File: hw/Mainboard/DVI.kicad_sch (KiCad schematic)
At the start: 18 parts, among them J12 NOT_HDMI_A

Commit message: hw: routing / silk wip
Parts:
- removed JP7: DVI_CEC, Jumper:SolderJumper-2_P1.3mm_Open_RoundedPad1.0x1.5mm, symbol Jumper:SolderJumper_2_Open
- removed JP8: DVI_SCL, Jumper:SolderJumper-2_P1.3mm_Open_RoundedPad1.0x1.5mm, symbol Jumper:SolderJumper_2_Open
- removed JP9: DVI_SDA, Jumper:SolderJumper-2_P1.3mm_Open_RoundedPad1.0x1.5mm, symbol Jumper:SolderJumper_2_Open
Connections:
- net HDMI_SCL is gone; now on net SCL: J12.15 (SCL), R8.2
- net HDMI_SDA is gone; now on net SDA: J12.16 (SDA), R9.2
- net CEC: now also R16.1, R7.2
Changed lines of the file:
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@@
-    (stroke (width 0) (type default) (color 0 0 0 0))
-  )
-  (wire (pts (xy 111.76 101.6) (xy 129.54 101.6))
     (stroke (width 0) (type default) (color 0 0 0 0))
   )
@@
     (stroke (width 0) (type default) (color 0 0 0 0))
   )
-  (wire (pts (xy 111.76 91.44) (xy 124.46 91.44))
-    (stroke (width 0) (type default) (color 0 0 0 0))
-  )
   (wire (pts (xy 167.64 68.58) (xy 180.34 68.58))
     (stroke (width 0) (type default) (color 0 0 0 0))
   )
-  (wire (pts (xy 97.79 101.6) (xy 104.14 101.6))
+  (wire (pts (xy 97.79 101.6) (xy 129.54 101.6))
     (stroke (width 0) (type default) (color 0 0 0 0))
   )
@@
     (stroke (width 0) (type default) (color 0 0 0 0))
   )
-  (wire (pts (xy 97.79 111.76) (xy 104.14 111.76))
-    (stroke (width 0) (type default) (color 0 0 0 0))
-  )
   (bus (pts (xy 146.05 66.04) (xy 146.05 68.58))
     (stroke (width 0) (type default) (color 0 0 0 0))
@@
     (stroke (width 0) (type default) (color 0 0 0 0))
   )
-  (wire (pts (xy 111.76 111.76) (xy 134.62 111.76))
+  (wire (pts (xy 97.79 111.76) (xy 134.62 111.76))
     (stroke (width 0) (type default) (color 0 0 0 0))
   )
@@
     (stroke (width 0) (type default) (color 0 0 0 0))
   )
-  (wire (pts (xy 97.79 91.44) (xy 104.14 91.44))
+  (wire (pts (xy 97.79 91.44) (xy 124.46 91.44))
     (stroke (width 0) (type default) (color 0 0 0 0))
   )
@@
     )
     (pin "1")
-  )
-  (symbol (lib_id "Jumper:SolderJumper_2_Open") (at 107.95 101.6 0) (unit 1)
-    (in_bom yes) (on_board yes) (fields_autoplaced)
-    (property "Reference" "JP8" (id 0) (at 107.95 95.25 0))
-    (property "Value" "DVI_SCL" (id 1) (at 107.95 97.79 0))
-    (property "Footprint" "Jumper:SolderJumper-2_P1.3mm_Open_RoundedPad1.0x1.5mm" (id 2) (at 107.95 101.6 0)
-      (effects (font (size 1.27 1.27)) hide)
-    )
-    (property "Datasheet" "~" (id 3) (at 107.95 101.6 0)
-      (effects (font (size 1.27 1.27)) hide)
-    )
-    (pin "1")
-    (pin "2")
   )
   (symbol (lib_id "PET:PowerTie_2") (at 194.31 59.69 180) (unit 1)
@@
     (pin "2")
   )
-  (symbol (lib_id "Jumper:SolderJumper_2_Open") (at 107.95 91.44 0) (unit 1)
-    (in_bom yes) (on_board yes) (fields_autoplaced)
-    (property "Reference" "JP7" (id 0) (at 107.95 85.09 0))
-    (property "Value" "DVI_CEC" (id 1) (at 107.95 87.63 0))
-    (property "Footprint" "Jumper:SolderJumper-2_P1.3mm_Open_RoundedPad1.0x1.5mm" (id 2) (at 107.95 91.44 0)
-      (effects (font (size 1.27 1.27)) hide)
-    )
-    (property "Datasheet" "~" (id 3) (at 107.95 91.44 0)
-      (effects (font (size 1.27 1.27)) hide)
-    )
-    (pin "1")
-    (pin "2")
-  )
   (symbol (lib_id "Device:R_Small") (at 165.1 86.36 90) (unit 1)
     (in_bom yes) (on_board yes)
@@
       (effects (font (size 1.27 1.27)) hide)
     )
-    (pin "1")
-    (pin "2")
-  )
-  (symbol (lib_id "Jumper:SolderJumper_2_Open") (at 107.95 111.76 0) (unit 1)
-    (in_bom yes) (on_board yes) (fields_autoplaced)
-    (property "Reference" "JP9" (id 0) (at 107.95 105.41 0))
-    (property "Value" "DVI_SDA" (id 1) (at 107.95 107.95 0))
-    (property "Footprint" "Jumper:SolderJumper-2_P1.3mm_Open_RoundedPad1.0x1.5mm" (id 2) (at 107.95 111.76 0)
-      (effects (font (size 1.27 1.27)) hide)
-    )
-    (property "Datasheet" "~" (id 3) (at 107.95 111.76 0)
-      (effects (font (size 1.27 1.27)) hide)
-    )

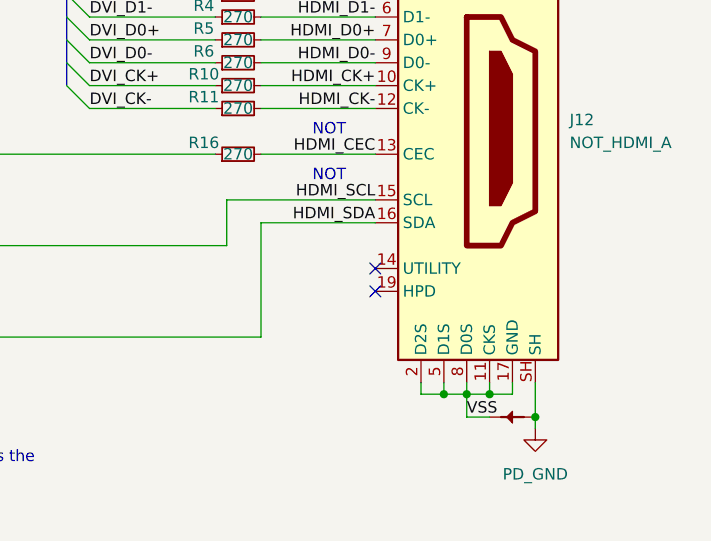
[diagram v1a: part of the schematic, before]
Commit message: hw: heat sink, trace size, more stitching
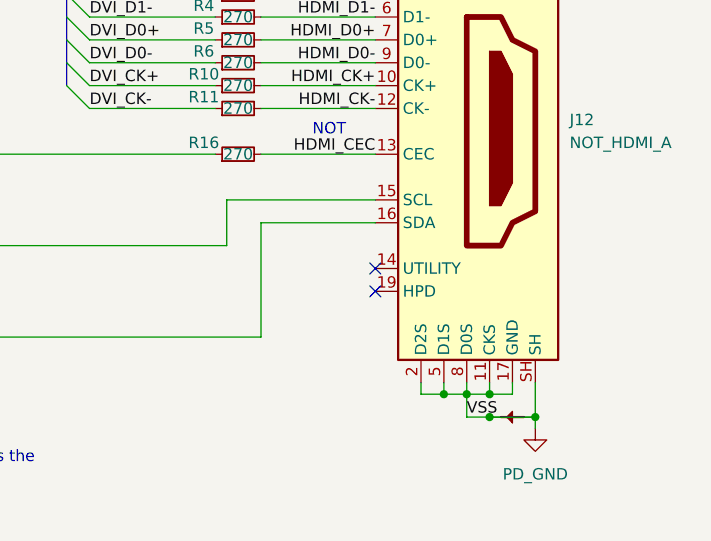
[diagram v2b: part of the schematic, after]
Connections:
- net VSS is gone; now on net PD_GND: J12.11 (CKS), J12.17 (GND), J12.2 (D2S), J12.5 (D1S), J12.8 (D0S), PT37.2
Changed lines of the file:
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@@
   (junction (at 134.62 111.76) (diameter 0) (color 0 0 0 0)
+  )
+  (junction (at 193.04 120.65) (diameter 0) (color 0 0 0 0)
   )
   (junction (at 193.04 118.11) (diameter 0) (color 0 0 0 0)
@@
     (stroke (width 0) (type default) (color 0 0 0 0))
   )
+  (wire (pts (xy 193.04 120.65) (xy 198.12 120.65))
+    (stroke (width 0) (type default) (color 0 0 0 0))
+  )
   (wire (pts (xy 163.83 101.6) (xy 163.83 96.52))
     (stroke (width 0) (type default) (color 0 0 0 0))
@@
   (wire (pts (xy 198.12 59.69) (xy 196.85 59.69))
     (stroke (width 0) (type default) (color 0 0 0 0))
-  )
-  (text "NOT" (at 173.355 94.615 0)
-    (effects (font (size 1.27 1.27)) (justify left bottom))
   )
   (text "NOT" (at 172.72 66.675 0)
@@
     (effects (font (size 1.27 1.27)) (justify right bottom))
   )
-  (label "HDMI_SCL" (at 180.34 96.52 180)
-    (effects (font (size 1.27 1.27)) (justify right bottom))
-  )
   (label "VSS" (at 190.5 120.65 0)
     (effects (font (size 1.27 1.27)) (justify left bottom))
@@
     (effects (font (size 1.27 1.27)) (justify left bottom))
   )
-  (label "HDMI_SDA" (at 180.34 99.06 180)
-    (effects (font (size 1.27 1.27)) (justify right bottom))
-  )
   (label "HDMI_D2+" (at 180.34 68.58 180)

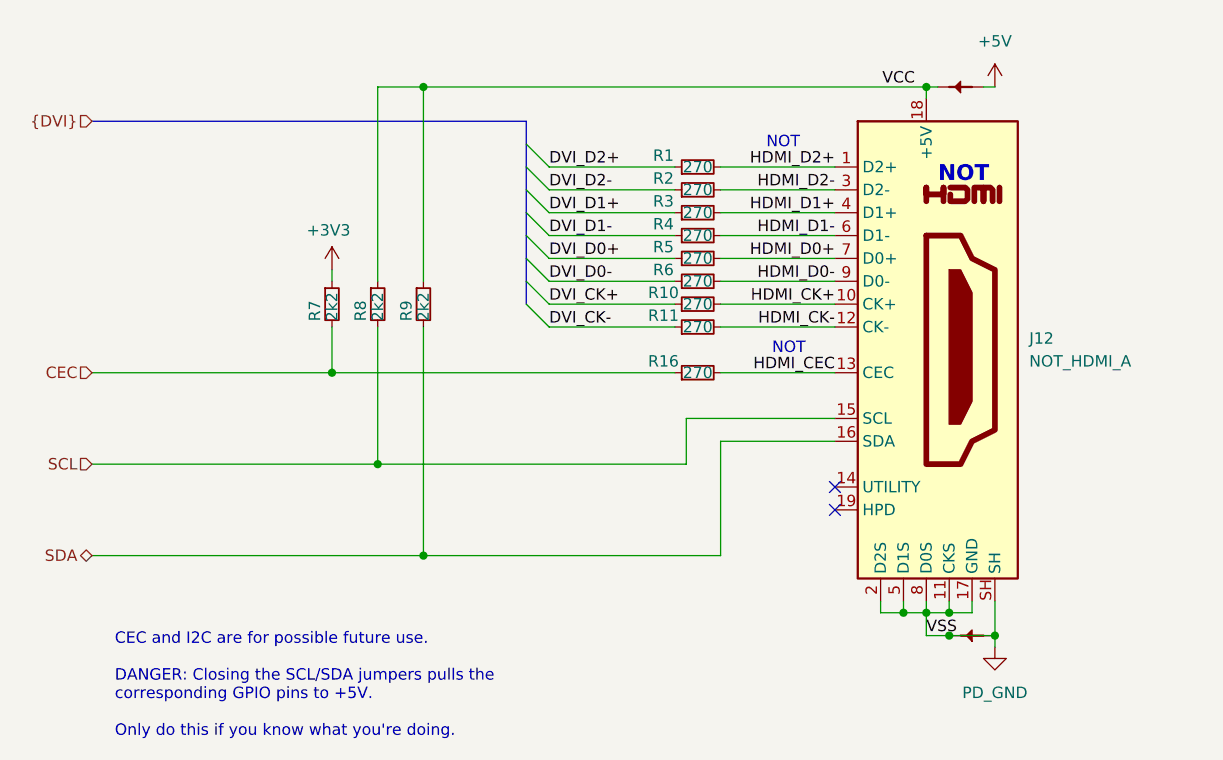
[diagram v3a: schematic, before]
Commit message: hw: 9V DC plug on left edge, change default track size
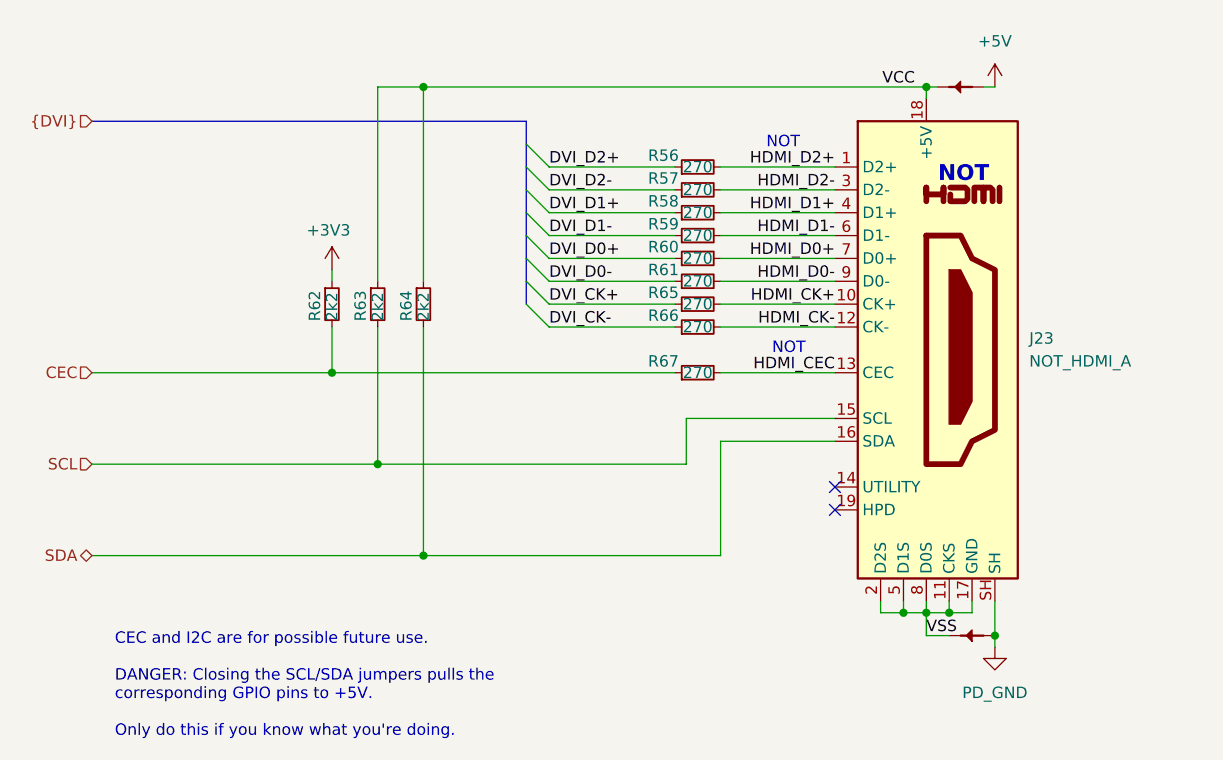
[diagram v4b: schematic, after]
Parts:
- renumbered J12 to J23, PT18 to PT49, PT37 to PT50, R1 to R56, R2 to R57, R3 to R58, R4 to R59, R5 to R60, R6 to R61, R7 to R62, R8 to R63, R9 to R64, R10 to R65, R11 to R66, R16 to R67
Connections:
- net PD_GND: no longer J23.11 (CKS), J23.17 (GND), J23.2 (D2S), J23.5 (D1S), J23.8 (D0S), PT50.2
- new net VSS: J23.11 (CKS), J23.17 (GND), J23.2 (D2S), J23.5 (D1S), J23.8 (D0S), PT50.2
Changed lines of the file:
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@@
   (junction (at 134.62 111.76) (diameter 0) (color 0 0 0 0)
-  )
-  (junction (at 193.04 120.65) (diameter 0) (color 0 0 0 0)
   )
   (junction (at 193.04 118.11) (diameter 0) (color 0 0 0 0)
@@
     (stroke (width 0) (type default) (color 0 0 0 0))
   )
-  (wire (pts (xy 193.04 120.65) (xy 198.12 120.65))
-    (stroke (width 0) (type default) (color 0 0 0 0))
-  )
   (wire (pts (xy 163.83 101.6) (xy 163.83 96.52))
     (stroke (width 0) (type default) (color 0 0 0 0))
@@
   (symbol (lib_id "Device:R_Small") (at 165.1 83.82 90) (unit 1)
     (in_bom yes) (on_board yes)
-    (property "Reference" "R10" (id 0) (at 161.29 82.55 90))
+    (property "Reference" "R65" (id 0) (at 161.29 82.55 90))
     (property "Value" "270" (id 1) (at 165.1 83.82 90))
     (property "Footprint" "Resistor_SMD:R_0603_1608Metric" (id 2) (at 165.1 83.82 0)
@@
   (symbol (lib_id "Device:R_Small") (at 165.1 76.2 90) (unit 1)
     (in_bom yes) (on_board yes)
-    (property "Reference" "R4" (id 0) (at 161.29 74.93 90))
+    (property "Reference" "R59" (id 0) (at 161.29 74.93 90))
     (property "Value" "270" (id 1) (at 165.1 76.2 90))
     (property "Footprint" "Resistor_SMD:R_0603_1608Metric" (id 2) (at 165.1 76.2 0)
@@
   (symbol (lib_id "Device:R_Small") (at 134.62 83.82 0) (unit 1)
     (in_bom yes) (on_board yes)
-    (property "Reference" "R9" (id 0) (at 132.715 85.725 90)
+    (property "Reference" "R64" (id 0) (at 132.715 85.725 90)
       (effects (font (size 1.27 1.27)) (justify left))
     )
@@
   (symbol (lib_id "PET:PowerTie_2") (at 195.58 120.65 180) (unit 1)
     (in_bom yes) (on_board yes) (fields_autoplaced)
-    (property "Reference" "PT37" (id 0) (at 195.58 122.555 0)
+    (property "Reference" "PT50" (id 0) (at 195.58 122.555 0)
       (effects (font (size 1.27 1.27)) hide)
     )
@@
   (symbol (lib_id "Device:R_Small") (at 129.54 83.82 0) (unit 1)
     (in_bom yes) (on_board yes)
-    (property "Reference" "R8" (id 0) (at 127.635 85.725 90)
+    (property "Reference" "R63" (id 0) (at 127.635 85.725 90)
       (effects (font (size 1.27 1.27)) (justify left))
     )
@@
   (symbol (lib_id "power:+5V") (at 198.12 59.69 0) (unit 1)
     (in_bom yes) (on_board yes) (fields_autoplaced)
-    (property "Reference" "#PWR0144" (id 0) (at 198.12 63.5 0)
+    (property "Reference" "#PWR0141" (id 0) (at 198.12 63.5 0)
       (effects (font (size 1.27 1.27)) hide)
     )
@@
   (symbol (lib_id "PET:PowerTie_2") (at 194.31 59.69 180) (unit 1)
     (in_bom yes) (on_board yes) (fields_autoplaced)
-    (property "Reference" "PT18" (id 0) (at 194.31 61.595 0)
+    (property "Reference" "PT49" (id 0) (at 194.31 61.595 0)
       (effects (font (size 1.27 1.27)) hide)
     )
@@
   (symbol (lib_id "power:+3V3") (at 124.46 80.01 0) (mirror y) (unit 1)
     (in_bom yes) (on_board yes)
-    (property "Reference" "#PWR0145" (id 0) (at 124.46 83.82 0)
+    (property "Reference" "#PWR0142" (id 0) (at 124.46 83.82 0)
       (effects (font (size 1.27 1.27)) hide)
     )
@@
   (symbol (lib_id "Connector:HDMI_A") (at 190.5 88.9 0) (unit 1)
     (in_bom yes) (on_board yes)
-    (property "Reference" "J12" (id 0) (at 201.93 87.63 0)
+    (property "Reference" "J23" (id 0) (at 201.93 87.63 0)
       (effects (font (size 1.27 1.27)) (justify left))
     )
@@
   (symbol (lib_id "Device:R_Small") (at 165.1 68.58 90) (unit 1)
     (in_bom yes) (on_board yes)
-    (property "Reference" "R1" (id 0) (at 161.29 67.31 90))
+    (property "Reference" "R56" (id 0) (at 161.29 67.31 90))
     (property "Value" "270" (id 1) (at 165.1 68.58 90))
     (property "Footprint" "Resistor_SMD:R_0603_1608Metric" (id 2) (at 165.1 68.58 0)
@@
   (symbol (lib_id "Device:R_Small") (at 165.1 91.44 90) (unit 1)
     (in_bom yes) (on_board yes)
-    (property "Reference" "R16" (id 0) (at 161.29 90.17 90))
+    (property "Reference" "R67" (id 0) (at 161.29 90.17 90))
     (property "Value" "270" (id 1) (at 165.1 91.44 90))
     (property "Footprint" "Resistor_SMD:R_0603_1608Metric" (id 2) (at 165.1 91.44 0)
@@
   (symbol (lib_id "Device:R_Small") (at 165.1 81.28 90) (unit 1)
     (in_bom yes) (on_board yes)
-    (property "Reference" "R6" (id 0) (at 161.29 80.01 90))
+    (property "Reference" "R61" (id 0) (at 161.29 80.01 90))
     (property "Value" "270" (id 1) (at 165.1 81.28 90))
     (property "Footprint" "Resistor_SMD:R_0603_1608Metric" (id 2) (at 165.1 81.28 0)
@@
   (symbol (lib_id "Device:R_Small") (at 165.1 86.36 90) (unit 1)
     (in_bom yes) (on_board yes)
-    (property "Reference" "R11" (id 0) (at 161.29 85.09 90))
+    (property "Reference" "R66" (id 0) (at 161.29 85.09 90))
     (property "Value" "270" (id 1) (at 165.1 86.36 90))
     (property "Footprint" "Resistor_SMD:R_0603_1608Metric" (id 2) (at 165.1 86.36 0)
@@
   (symbol (lib_id "Device:R_Small") (at 165.1 78.74 90) (unit 1)
     (in_bom yes) (on_board yes)
-    (property "Reference" "R5" (id 0) (at 161.29 77.47 90))
+    (property "Reference" "R60" (id 0) (at 161.29 77.47 90))
     (property "Value" "270" (id 1) (at 165.1 78.74 90))
     (property "Footprint" "Resistor_SMD:R_0603_1608Metric" (id 2) (at 165.1 78.74 0)
@@
   (symbol (lib_id "Device:R_Small") (at 124.46 83.82 0) (unit 1)
     (in_bom yes) (on_board yes)
-    (property "Reference" "R7" (id 0) (at 122.555 85.725 90)
+    (property "Reference" "R62" (id 0) (at 122.555 85.725 90)
       (effects (font (size 1.27 1.27)) (justify left))
     )
@@
   (symbol (lib_id "PET:PD_GND") (at 198.12 121.92 0) (unit 1)
     (in_bom yes) (on_board yes) (fields_autoplaced)
-    (property "Reference" "#PWR0146" (id 0) (at 198.12 128.27 0)
+    (property "Reference" "#PWR0143" (id 0) (at 198.12 128.27 0)
       (effects (font (size 1.27 1.27)) hide)
     )
@@
   (symbol (lib_id "Device:R_Small") (at 165.1 71.12 90) (unit 1)
     (in_bom yes) (on_board yes)
-    (property "Reference" "R2" (id 0) (at 161.29 69.85 90))
+    (property "Reference" "R57" (id 0) (at 161.29 69.85 90))
     (property "Value" "270" (id 1) (at 165.1 71.12 90))
     (property "Footprint" "Resistor_SMD:R_0603_1608Metric" (id 2) (at 165.1 71.12 0)
@@
   (symbol (lib_id "Device:R_Small") (at 165.1 73.66 90) (unit 1)
     (in_bom yes) (on_board yes)
-    (property "Reference" "R3" (id 0) (at 161.29 72.39 90))
+    (property "Reference" "R58" (id 0) (at 161.29 72.39 90))
     (property "Value" "270" (id 1) (at 165.1 73.66 90))
     (property "Footprint" "Resistor_SMD:R_0603_1608Metric" (id 2) (at 165.1 73.66 0)

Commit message: hw: 25x2 header (wip)
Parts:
- renumbered J23 to J24
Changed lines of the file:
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@@
   (symbol (lib_id "power:+5V") (at 198.12 59.69 0) (unit 1)
     (in_bom yes) (on_board yes) (fields_autoplaced)
-    (property "Reference" "#PWR0141" (id 0) (at 198.12 63.5 0)
+    (property "Reference" "#PWR0143" (id 0) (at 198.12 63.5 0)
       (effects (font (size 1.27 1.27)) hide)
     )
@@
   (symbol (lib_id "power:+3V3") (at 124.46 80.01 0) (mirror y) (unit 1)
     (in_bom yes) (on_board yes)
-    (property "Reference" "#PWR0142" (id 0) (at 124.46 83.82 0)
+    (property "Reference" "#PWR0144" (id 0) (at 124.46 83.82 0)
       (effects (font (size 1.27 1.27)) hide)
     )
@@
   (symbol (lib_id "Connector:HDMI_A") (at 190.5 88.9 0) (unit 1)
     (in_bom yes) (on_board yes)
-    (property "Reference" "J23" (id 0) (at 201.93 87.63 0)
+    (property "Reference" "J24" (id 0) (at 201.93 87.63 0)
       (effects (font (size 1.27 1.27)) (justify left))
     )
@@
   (symbol (lib_id "PET:PD_GND") (at 198.12 121.92 0) (unit 1)
     (in_bom yes) (on_board yes) (fields_autoplaced)
-    (property "Reference" "#PWR0143" (id 0) (at 198.12 128.27 0)
+    (property "Reference" "#PWR0145" (id 0) (at 198.12 128.27 0)
       (effects (font (size 1.27 1.27)) hide)
     )

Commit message: hw: 2x config switch (wip)
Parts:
- renumbered J24 to J23
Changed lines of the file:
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@@
   (symbol (lib_id "power:+5V") (at 198.12 59.69 0) (unit 1)
     (in_bom yes) (on_board yes) (fields_autoplaced)
-    (property "Reference" "#PWR0143" (id 0) (at 198.12 63.5 0)
+    (property "Reference" "#PWR0149" (id 0) (at 198.12 63.5 0)
       (effects (font (size 1.27 1.27)) hide)
     )
@@
   (symbol (lib_id "power:+3V3") (at 124.46 80.01 0) (mirror y) (unit 1)
     (in_bom yes) (on_board yes)
-    (property "Reference" "#PWR0144" (id 0) (at 124.46 83.82 0)
+    (property "Reference" "#PWR0150" (id 0) (at 124.46 83.82 0)
       (effects (font (size 1.27 1.27)) hide)
     )
@@
   (symbol (lib_id "Connector:HDMI_A") (at 190.5 88.9 0) (unit 1)
     (in_bom yes) (on_board yes)
-    (property "Reference" "J24" (id 0) (at 201.93 87.63 0)
+    (property "Reference" "J23" (id 0) (at 201.93 87.63 0)
       (effects (font (size 1.27 1.27)) (justify left))
     )
@@
   (symbol (lib_id "PET:PD_GND") (at 198.12 121.92 0) (unit 1)
     (in_bom yes) (on_board yes) (fields_autoplaced)
-    (property "Reference" "#PWR0145" (id 0) (at 198.12 128.27 0)
+    (property "Reference" "#PWR0151" (id 0) (at 198.12 128.27 0)
       (effects (font (size 1.27 1.27)) hide)
     )

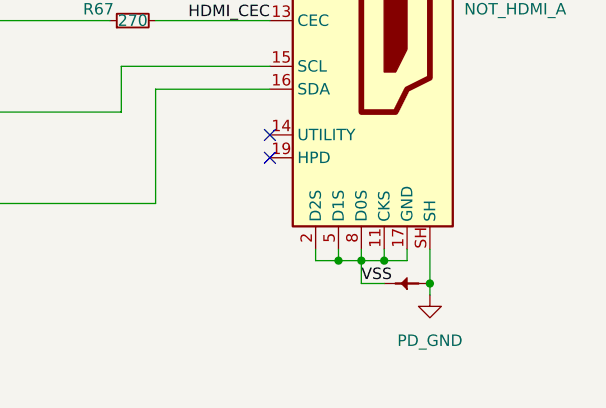
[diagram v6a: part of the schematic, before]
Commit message: hw: remove series termination, gnd under hdmi (wip)
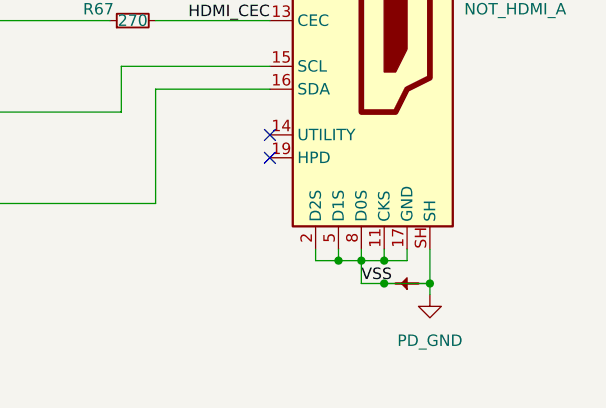
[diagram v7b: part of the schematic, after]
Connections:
- net VSS is gone; now on net PD_GND: J23.11 (CKS), J23.17 (GND), J23.2 (D2S), J23.5 (D1S), J23.8 (D0S), PT50.2
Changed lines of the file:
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@@
   (junction (at 134.62 111.76) (diameter 0) (color 0 0 0 0)
+  )
+  (junction (at 193.04 120.65) (diameter 0) (color 0 0 0 0)
   )
   (junction (at 193.04 118.11) (diameter 0) (color 0 0 0 0)
@@
     (stroke (width 0) (type default) (color 0 0 0 0))
   )
+  (wire (pts (xy 193.04 120.65) (xy 198.12 120.65))
+    (stroke (width 0) (type default) (color 0 0 0 0))
+  )
